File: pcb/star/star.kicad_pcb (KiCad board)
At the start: 2 copper layers, 50.7 x 48.4 mm, 36 parts, among them J1 POWER, J2 Conn_01x06_Male, SW1 RST, SW2 PRG, U1 ESP-12F, U2 AP2112K-3.3

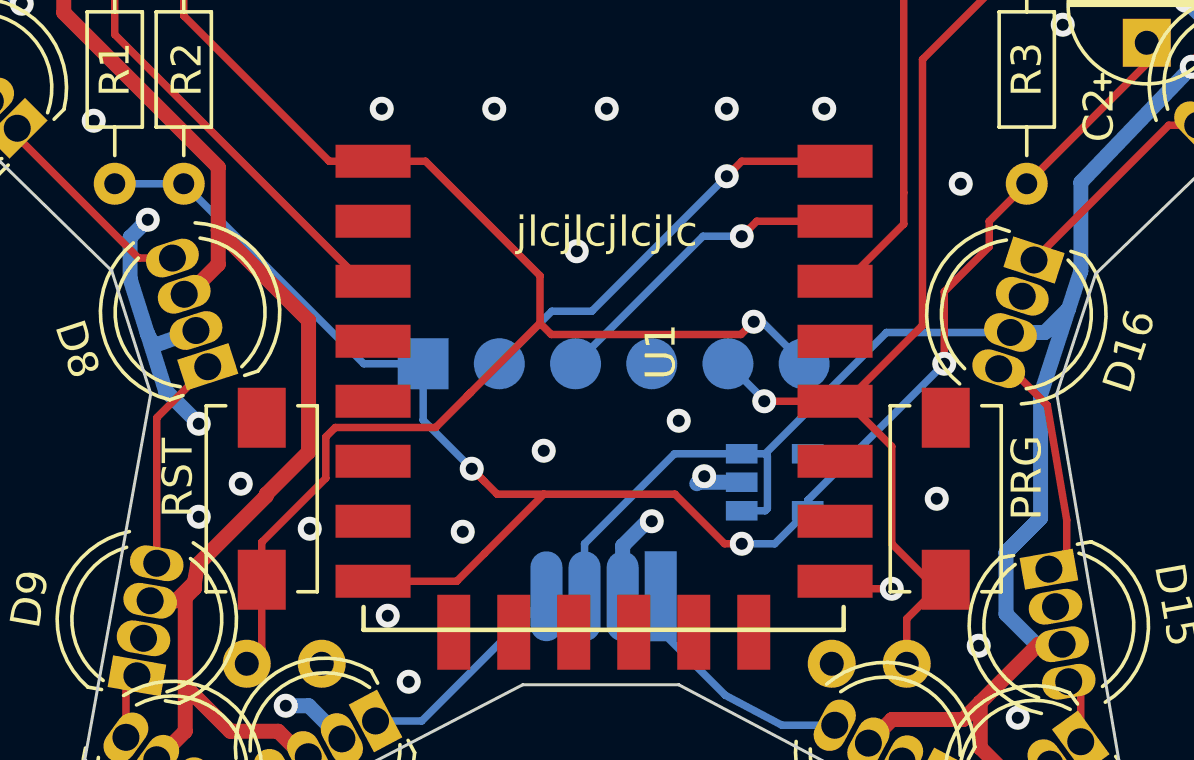
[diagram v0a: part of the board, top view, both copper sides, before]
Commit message: programmer and cad added
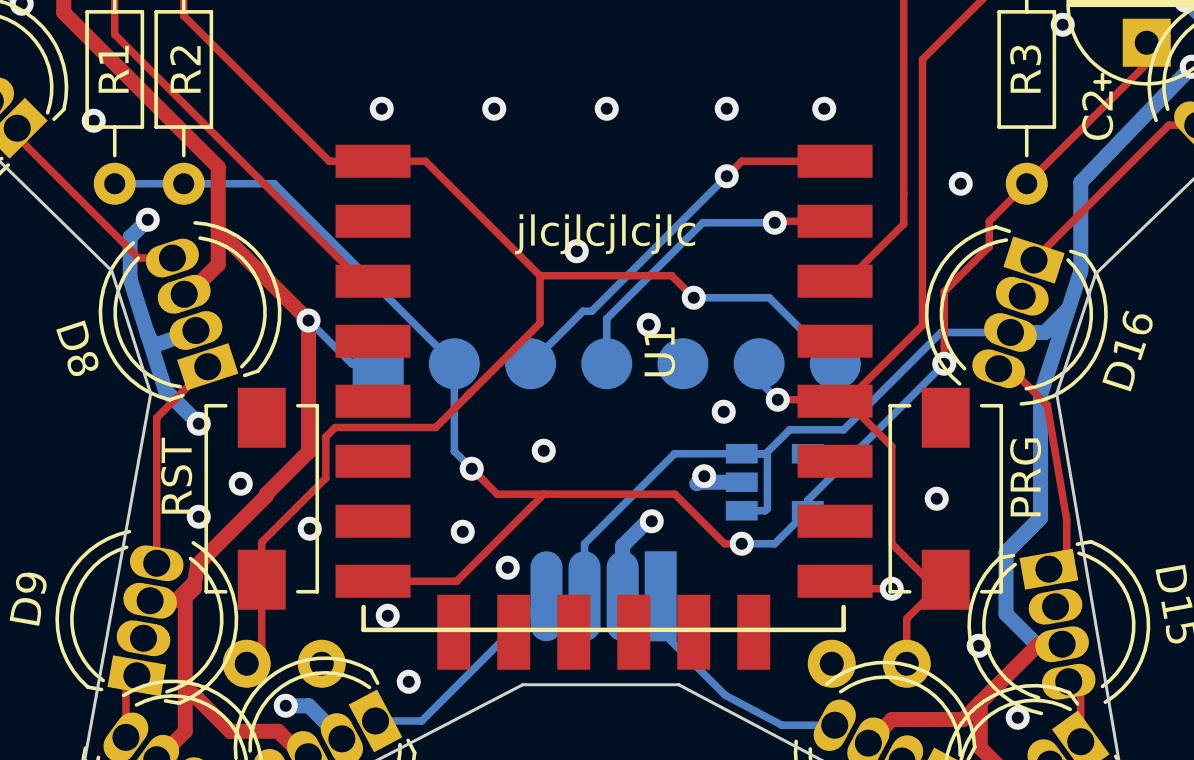
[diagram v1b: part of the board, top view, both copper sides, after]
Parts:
- J2: value Conn_01x06_Male -> program; footprint star:conn_01x06_SMD -> star:conn_01x07_SMD
- moved J2 0.23 mm to (98.0, 92.0)
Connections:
- net /ADC renamed Net-(U1-Pad2)
- J2 pad 1: +3V3 -> +5V
- J2 pad 2: /TXD -> +3V3
- J2 pad 3: /RXD -> /TXD
- J2 pad 4: GND -> /RXD
- J2 pad 5: /GPIO0 -> GND
- J2 pad 6: /RST -> /GPIO0
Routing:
- net +5V: track 197.9 -> 201.6 mm, vias 1 -> 2
- net /RST: track 46.3 -> 47.7 mm
- net /TXD: track 13.3 -> 12.2 mm
- net /GPIO0: track 32.9 -> 32.1 mm
- net +3V3: track 56.9 -> 57.5 mm
- net GND: vias 40 -> 42

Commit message: gergers generated
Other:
- board text added: "JLCJLCJLCJLC"
- board text removed: "jlcjlcjlcjlc"

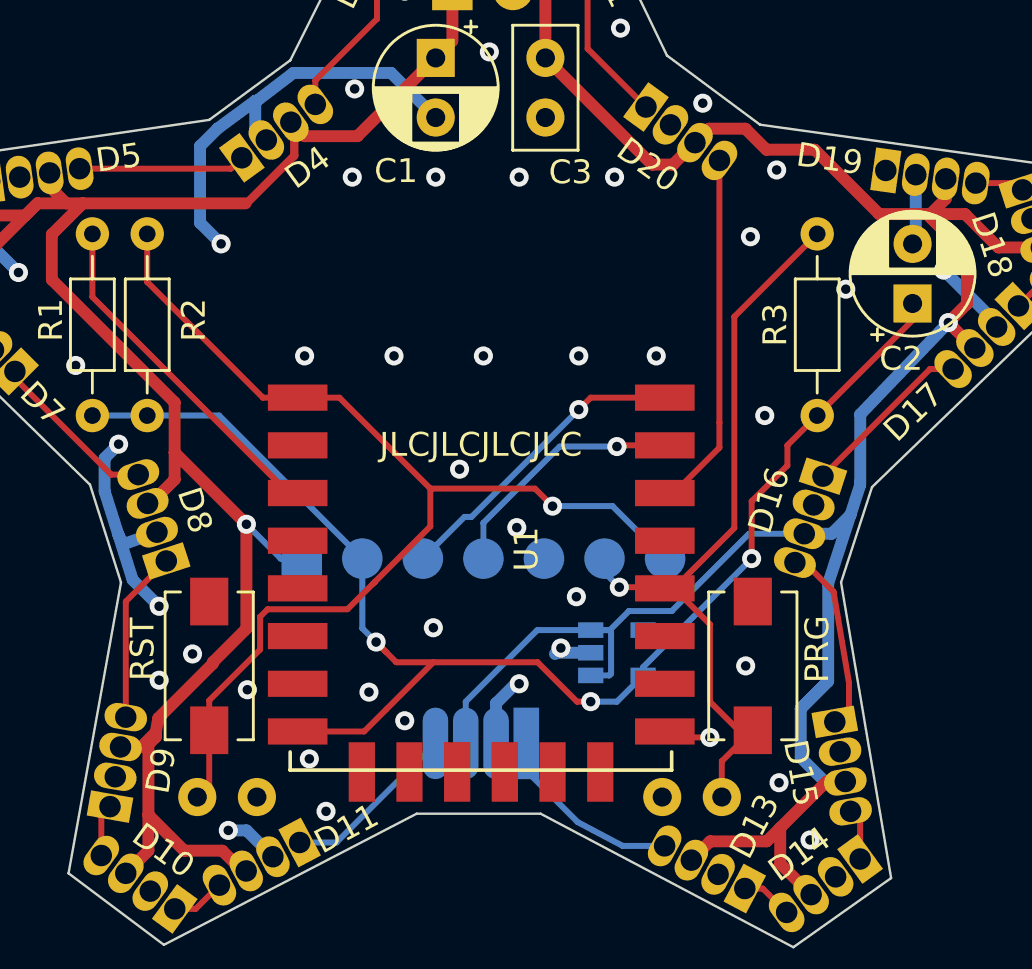
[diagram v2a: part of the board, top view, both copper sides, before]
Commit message: led pin changed to GPIO2
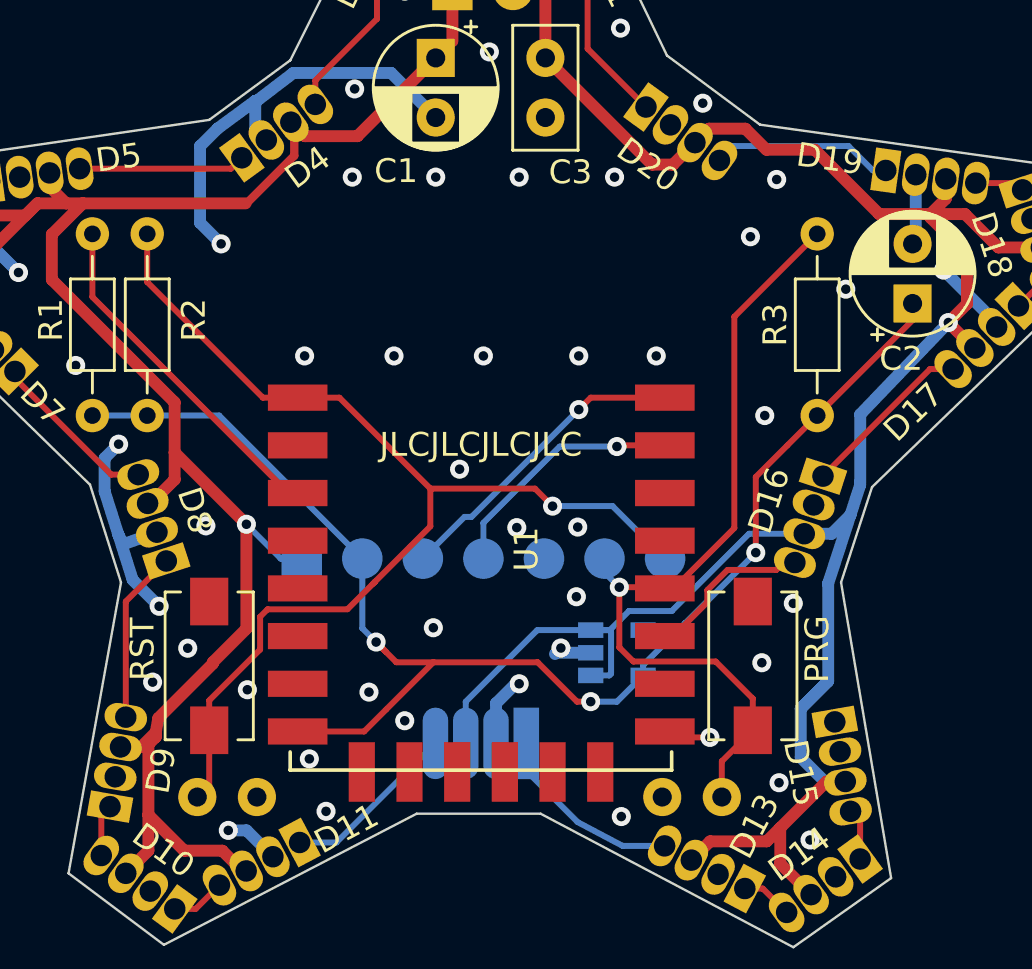
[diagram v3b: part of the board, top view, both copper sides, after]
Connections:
- net Net-(D1-Pad4) renamed /DoD20
- D15 pad 1: /DoD15 -> Net-(D15-Pad1)
- D16 pad 4: /DoD15 -> /LED_Din
- D20 pad 4: /LED_Din -> Net-(D19-Pad1)
- U1 pad 11: Net-(U1-Pad11) -> /LED_Din
- U1 pad 14: /LED_Din -> Net-(U1-Pad14)
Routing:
- net /DoD15: track 7.89 -> 0.00 mm
- net /LED_Din: track 15.8 -> 8.01 mm
- net Net-(D19-Pad1): track 0.00 -> 7.65 mm
- net /GPIO0: track 32.1 -> 34.8 mm
- net Net-(U1-Pad14): track 0.00 -> 1.09 mm
- net GND: vias 42 -> 46
